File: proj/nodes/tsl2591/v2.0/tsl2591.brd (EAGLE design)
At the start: 50.9 x 31.8 mm, 5 parts

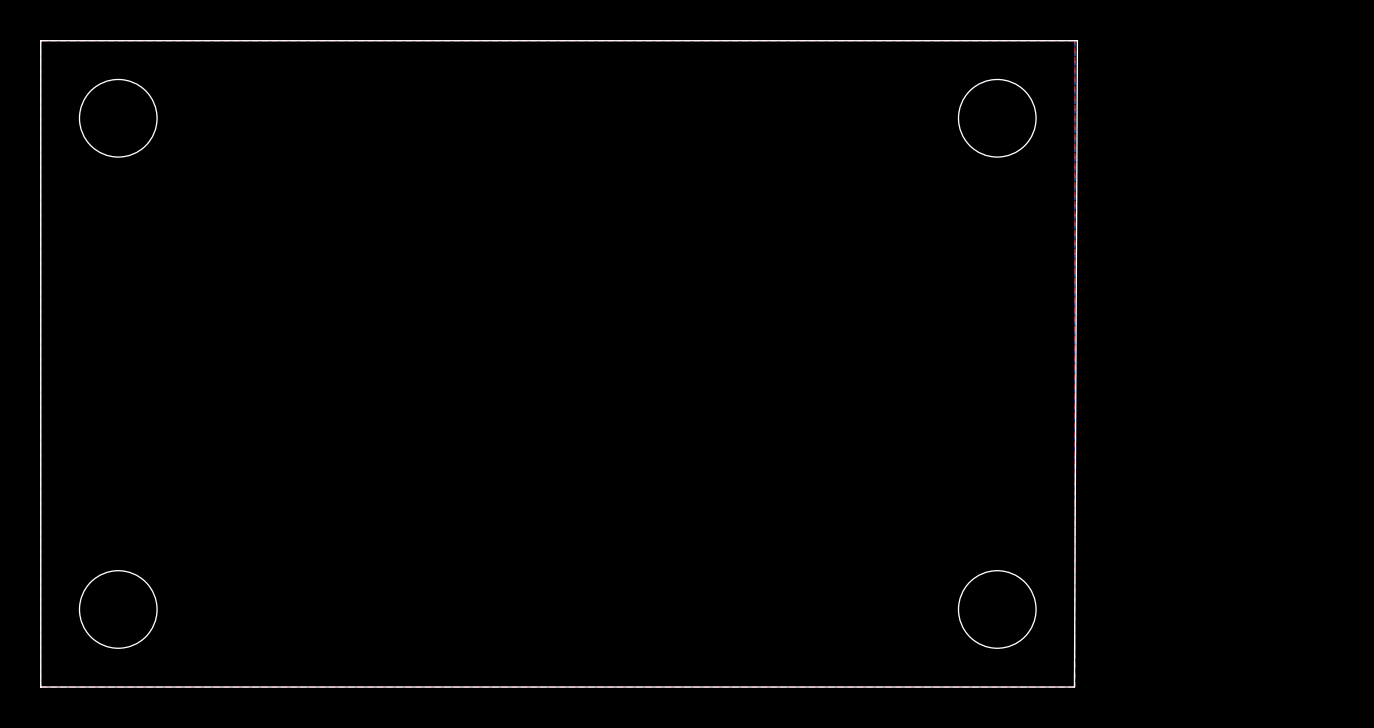
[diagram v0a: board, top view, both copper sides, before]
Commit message: cleaned up design blocks, added co2 sensor node v2.0
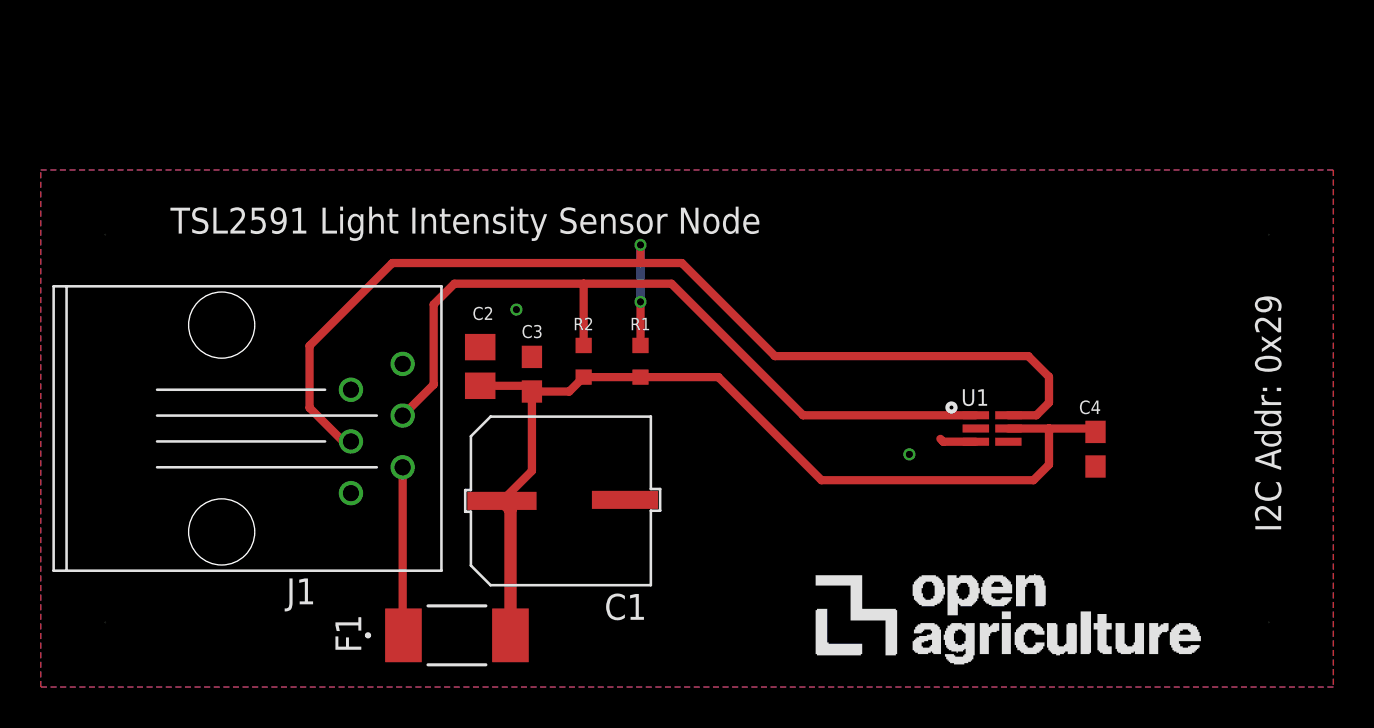
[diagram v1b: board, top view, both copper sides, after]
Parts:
- removed U$1, U$3, U$4: (no value), openag-frames:OPENAG-CORNER-MOUNTING-HOLE
- added C1: 100uF, openag-capacitors:EEE-1HA101UP
- added C2: 4.7uF, openag-capacitors:C0805
- added C3, C4: 0.1uF, openag-capacitors:C0603
- added F1: SST 7, openag-fuses:SS
- added J1: RJ12, openag-connectors:RJ12
- added R1, R2: 1K, openag-resistors:RC0603N
- added U1: TSL2591, openag-sensors:DFN6_TAOS
- U$2: device openag-frames:OPENAG-CORNER-MOUNTING-HOLE -> openag-frames:OPENAG-LOGO-750-MIL
- moved FRAME1 14.3 mm to (58.4, 3.17)
- moved U$2 9.18 mm to (38.1, 1.52), turned to 0 degrees
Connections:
- new net +3V3: C1.+, C2.1, C3.1, C4.1, F1.2, R1.2, R2.2, U1.5
- new net 3V3_IN: F1.1, J1.5
- new net 5V_IN: J1.6
- new net GND: C1.-, C2.2, C3.2, C4.2, J1.1, U1.3
- new net IO: J1.2
- new net SCL: J1.3, R2.1, U1.1
- new net SDA: J1.4, R1.1, U1.6
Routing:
- net SDA: track 0.00 -> 55.4 mm, vias 0 -> 2
- net +3V3: track 0.00 -> 49.7 mm
- net SCL: track 0.00 -> 38.9 mm
- net 3V3_IN: track 0.00 -> 8.27 mm
- net GND: track 0.00 -> 1.80 mm, vias 0 -> 2
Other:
- board outline removed
- board text added: "0.125""
- board text added: "0.75""
- board text added: "2.25""
- board text added: "I2C Addr: 0x29"
- board text added: "TSL2591 Light Intensity Sensor Node"
- board text added: "d=0.15""
